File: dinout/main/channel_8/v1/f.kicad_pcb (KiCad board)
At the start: 2 copper layers, 76.8 x 81.3 mm, 15 parts, among them J1 fm16_i, J10 data_manager_i, J11 wrs_i, J12 selector4_i, J13 bus_i, J2 0, J3 1, J4 2, J5 3, J6 4, J7 5, J8 6, J9 7

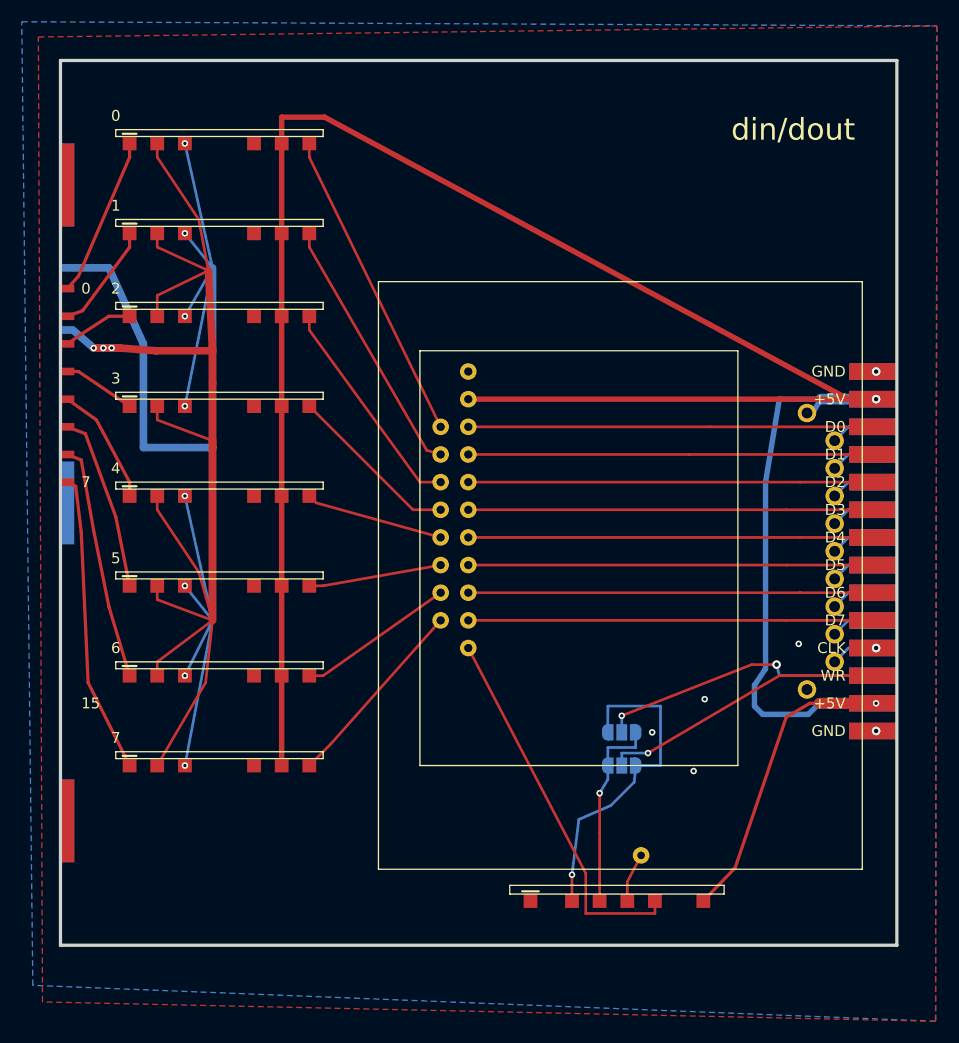
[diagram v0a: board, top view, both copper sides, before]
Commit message: voltage regulator for each module
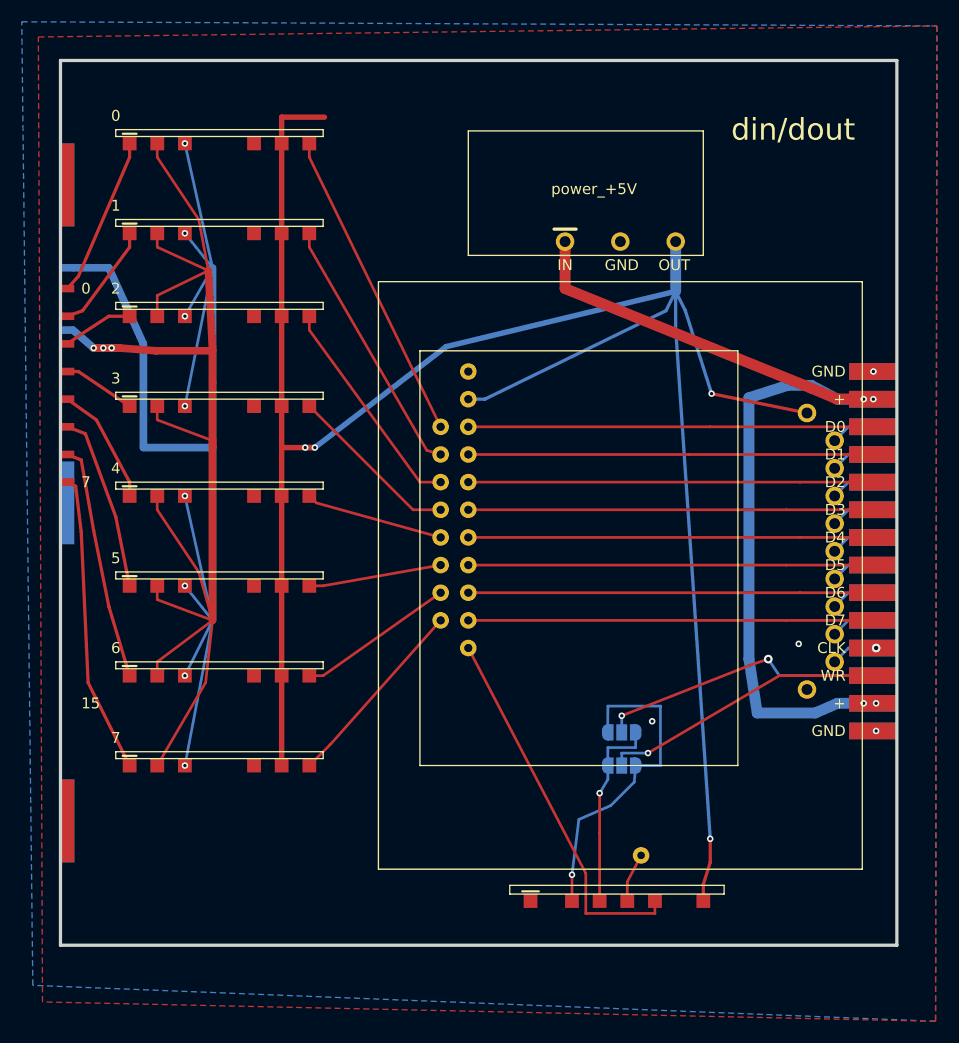
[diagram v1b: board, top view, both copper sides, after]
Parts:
- added J14: power_+5V, plc88:power_i, F.Cu at (-4.45, 0.13)
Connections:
- J13 pad 25: +5V -> VPBUS
- J13 pad 26: +5V -> VPBUS
- J13 pad 3: +5V -> VPBUS
- J13 pad 4: +5V -> VPBUS
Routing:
- net VPBUS: track 0.00 -> 86.7 mm, vias 0 -> 4
- net +5V: track 234.2 -> 206.6 mm, vias 2 -> 4
- net GND: vias 6 -> 4
